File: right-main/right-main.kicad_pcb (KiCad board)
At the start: 2 copper layers, 150.4 x 123.8 mm, 208 parts, among them J1 USBCONN, P1 CONN_4, P2 CONN_5, P3 CONN_6, SW1 PTS525SM10, SW11 SPST, SW12 SPST, SW13 SPST, SW14 SPST, SW15 SPST, SW16 SPST, SW17 SPST, SW21 SPST, SW22 SPST, SW23 SPST, SW24 SPST, SW25 SPST, SW26 SPST, SW27 SPST, SW31 SPST, SW32 SPST, SW33 SPST, SW34 SPST, SW35 SPST, SW36 SPST, SW37 SPST, SW41 SPST, SW42 SPST, SW43 SPST, SW44 SPST, SW45 SPST, SW46 SPST, SW47 SPST, SW52 SPST, SW53 SPST, SW54 SPST, SW55 SPST, SW56 SPST, SW57 SPST, U1 ATMEGA32U4, U2 CAT24C256, X1 16Mhz

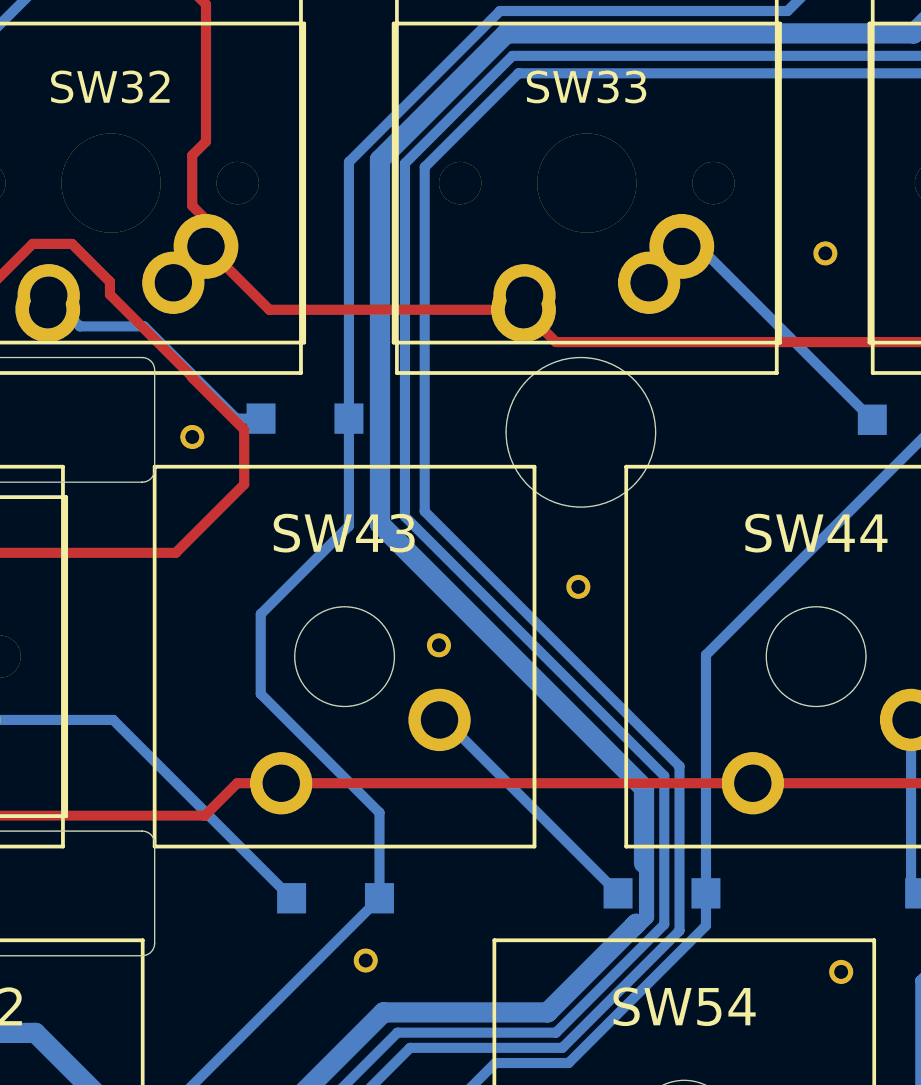
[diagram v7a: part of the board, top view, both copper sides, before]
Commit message: switch 43 right
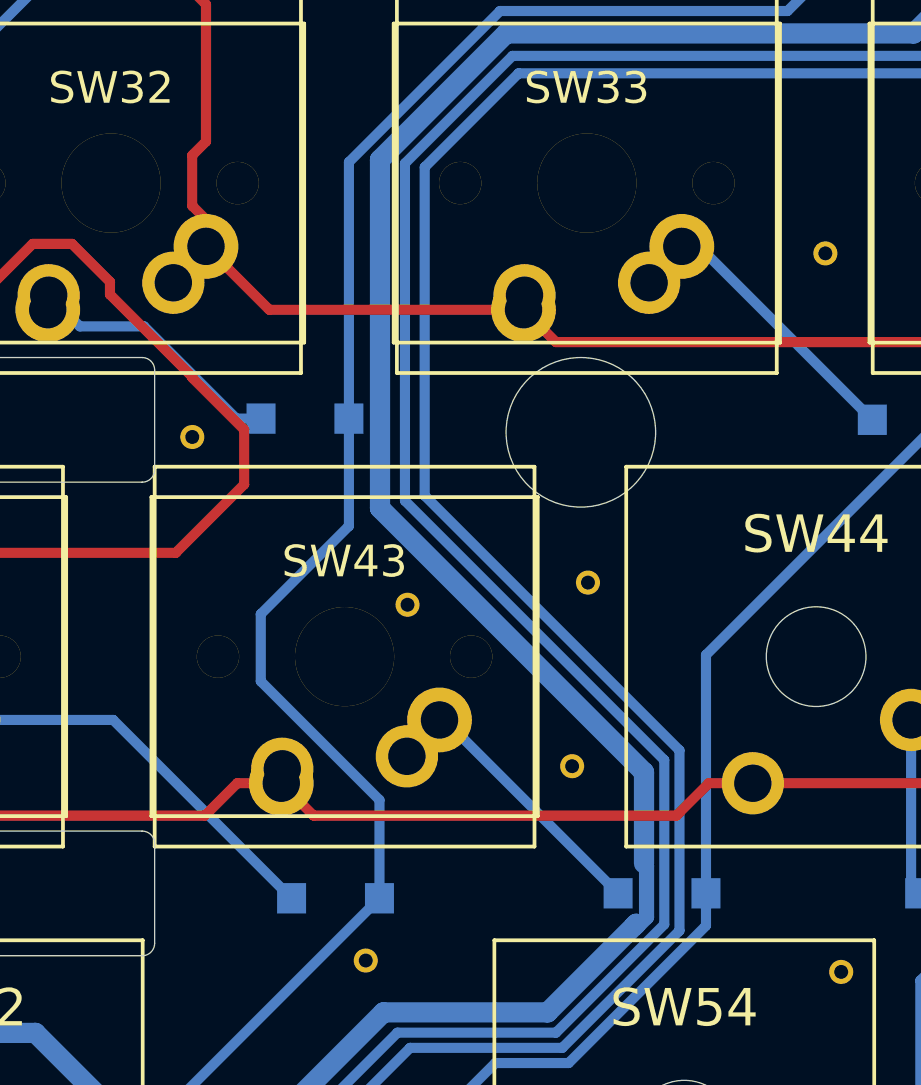
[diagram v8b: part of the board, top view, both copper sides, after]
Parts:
- added via 38/22mil: VAL**, ugl:via_38_22mil, F.Cu at (158.8, 125.1)
- SW43: footprint UGL:Cherry_MX -> ugl:Cherry-MX-Matias-Hybrid
- moved via 38/22mil 2.06 mm to (152.1, 118.6)
- moved via 38/22mil 0.42 mm to (159.4, 117.7)
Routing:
- net Net-(D43-Pad2): track 10.0 -> 12.0 mm
- net /ROW4: track 217.5 -> 218.3 mm
